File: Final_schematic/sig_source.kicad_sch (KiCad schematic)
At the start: 17 parts, among them U1 TL074, U5 MCP4561-502E_MS

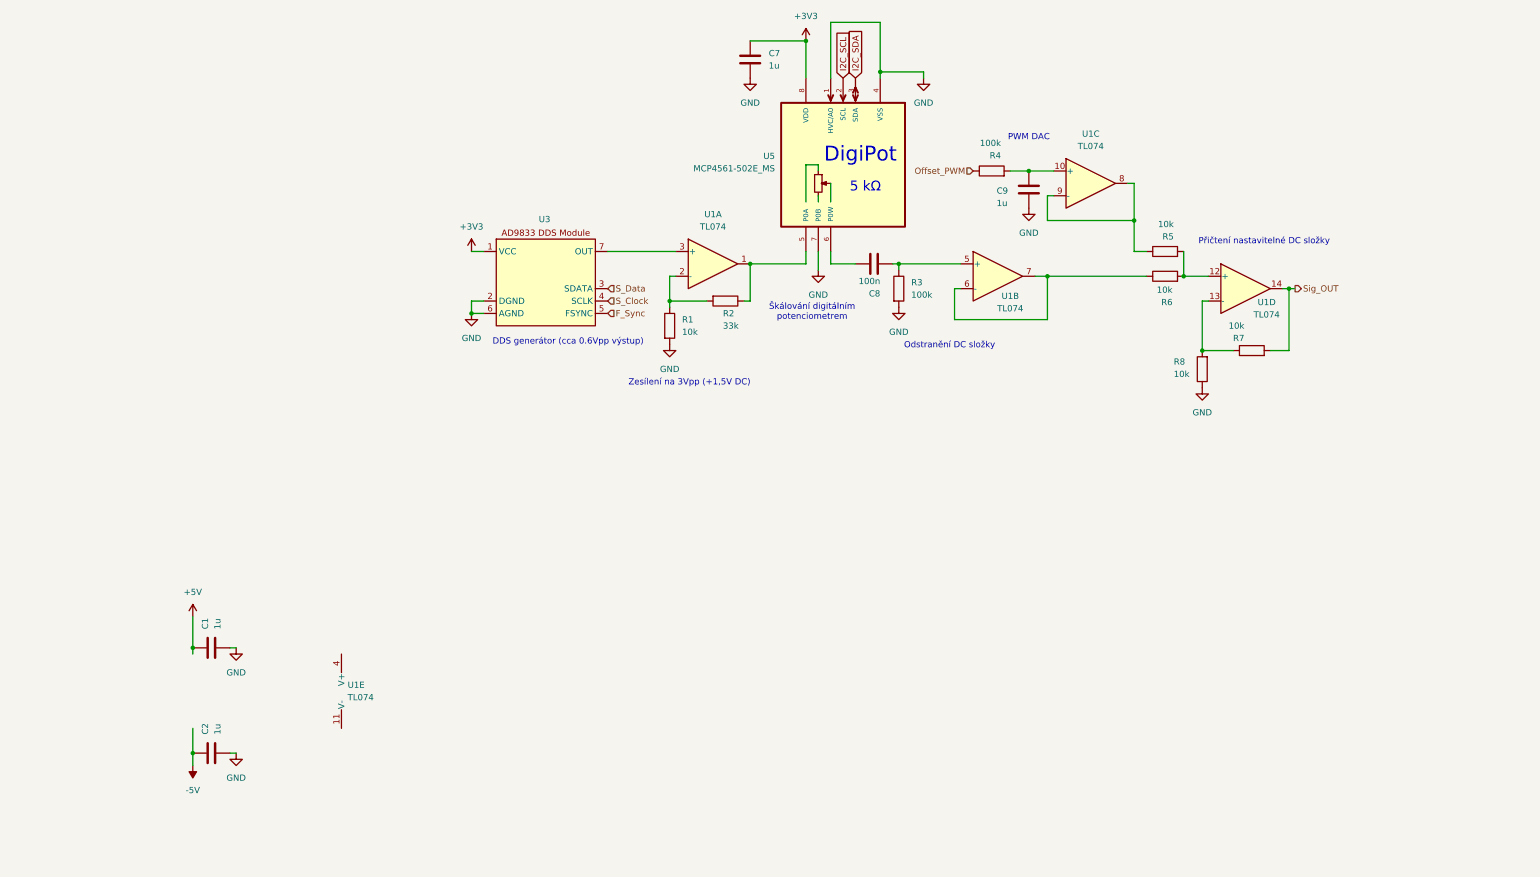
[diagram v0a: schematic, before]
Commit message: Removed obsolete PDF files and updated LaTeX documents with new sections and references.
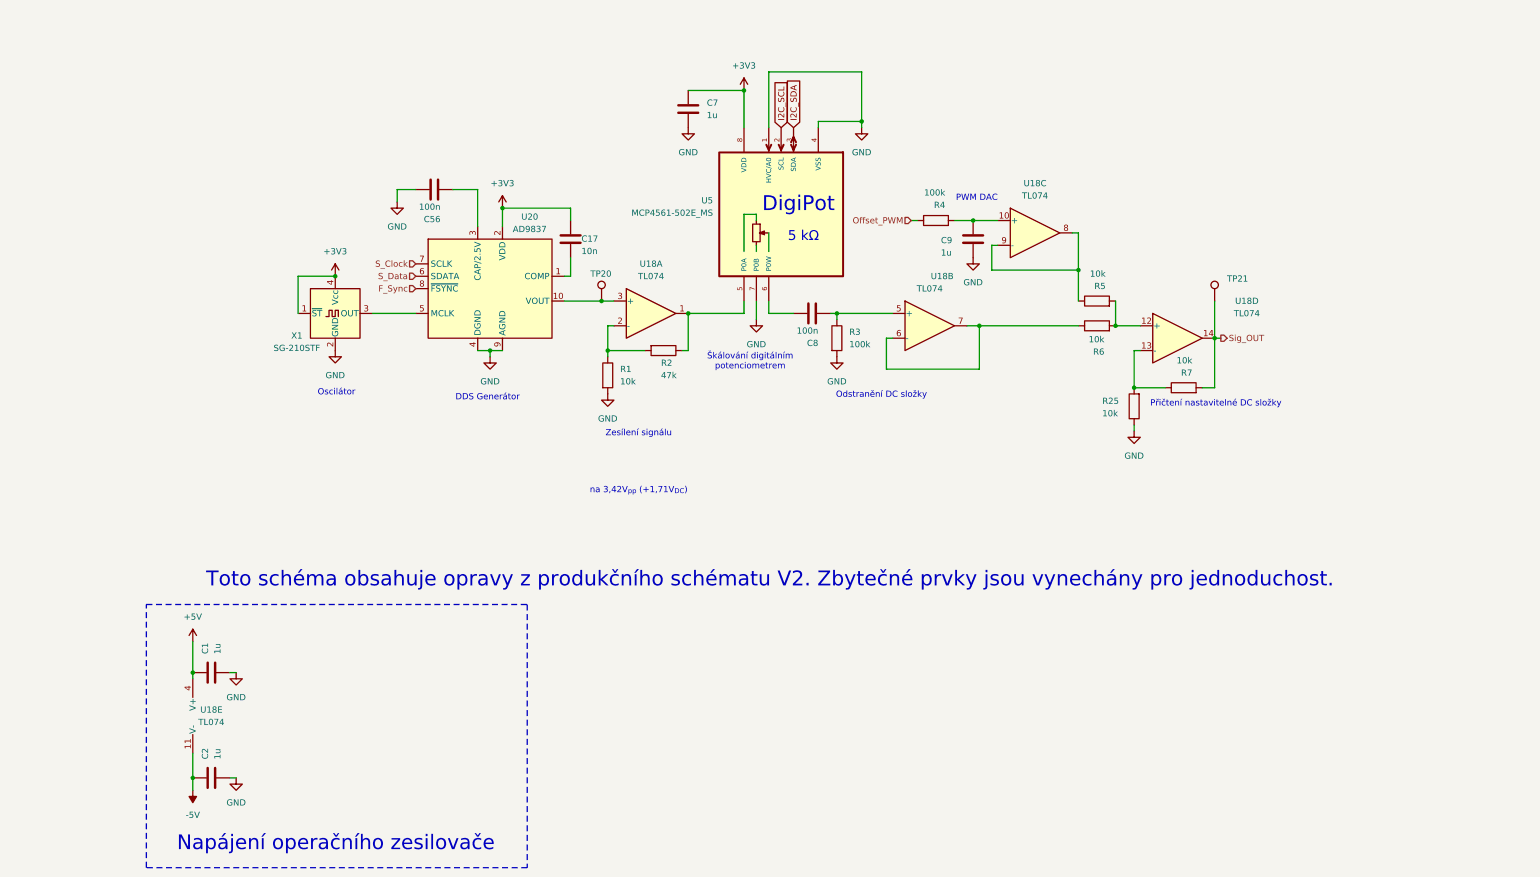
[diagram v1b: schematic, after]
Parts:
- removed R8: 10k, Resistor_SMD:R_0603_1608Metric_Pad0.98x0.95mm_HandSolder, symbol Device:R
- removed U1: TL074, symbol Amplifier_Operational:TL074
- removed U3: (no value), Snapeda:AD9833_Module, symbol Snapeda:AD9833_Module
- added C17: 10n, Capacitor_SMD:C_0603_1608Metric_Pad1.08x0.95mm_HandSolder, symbol Device:C
- added C56: 100n, Capacitor_SMD:C_0603_1608Metric_Pad1.08x0.95mm_HandSolder, symbol Device:C
- added R25: 10k, Resistor_SMD:R_0603_1608Metric_Pad0.98x0.95mm_HandSolder, symbol Device:R
- added TP20, TP21: TestPoint, Connector_Pin:Pin_D1.0mm_L10.0mm, symbol Connector:TestPoint
- added U18: TL074, Package_SO:TSSOP-14_4.4x5mm_P0.65mm, symbol Amplifier_Operational:TL074
- added U20: AD9837, Package_CSP:LFCSP-WD-10-1EP_3x3mm_P0.5mm_EP1.64x2.38mm, symbol Interface:AD9833xRM
- added X1: SG-210STF, Oscillator:Oscillator_SMD_SeikoEpson_SG210-4Pin_2.5x2.0mm, symbol Oscillator:SG-210STF
- R2: value 33k -> 47k
- U5: footprint Snapeda:MCP4561-502E_MS_SOP65P490X110-8N -> Package_SO:MSOP-8_3x3mm_P0.65mm
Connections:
- net +3V3: now also C17.1, U20.2 (VDD), X1.1 (~{ST}), X1.4 (Vcc)
- net +5V: now also U18.4 (V+)
- net -5V: now also U18.11 (V-)
- net F_Sync: now also U20.8 (~{FSYNC})
- net GND: now also C56.2, R25.1, U20.4 (DGND), U20.9 (AGND), X1.2 (GND)
- net S_Clock: now also U20.7 (SCLK)
- net S_Data: now also U20.6 (SDATA)
- net Sig_OUT: now also TP21.1, U18.14
- net at C9.2, R4.2: now also U18.10 (+)
- net at R5.2, R6.2: now also U18.12 (+)
- net at R7.1: now also R25.2, U18.13 (-)
- net at R5.1: now also U18.8, U18.9 (-)
- net at R2.1, U5.5 (P0A): now also U18.1
- net at R1.1, R2.2: now also U18.2 (-)
- net at R6.1: now also U18.6 (-), U18.7
- net at C8.1, R3.1: now also U18.5 (+)
- new net: C17.2, U20.1 (COMP)
- new net: TP20.1, U18.3 (+), U20.10 (VOUT)
- new net: C56.1, U20.3 (CAP/2.5V)
- new net: U20.5 (MCLK), X1.3 (OUT)
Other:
- note added: "DDS Generátor"
- note added: "Napájení operačního zesilovače"
- note added: "Oscilátor"
- note added: "Toto schéma obsahuje opravy z produkčního schématu V2. Zbytečné prvky jsou vynechány pro jednoduchost."
- note added: "Zesílení signálu"
- note added: "na 3,42V_{pp} (+1,71V_{DC})"
- note removed: "DDS generátor (cca 0.6Vpp výstup)"
- note removed: "Zesílení na 3Vpp (+1,5V DC)"
- moved on the sheet: C1, C2, C7, C8, C9, R1, R2, R3, R4, R5, R6, R7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
